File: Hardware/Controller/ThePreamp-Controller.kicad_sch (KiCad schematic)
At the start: 17 parts, among them J1 8V, J2 Digital Out, J3 SPI DISPLAY 1, J4 SPI DISPLAY 2, J5 Power relay trigger, SW1 RotaryEncoder_Switch, SW2 RotaryEncoder_Switch, U1 CAT24C64WI-GT3, U2 ESP32-DEVKIT-V1, U3 TSOP34838, U4 APC-817B1-SL

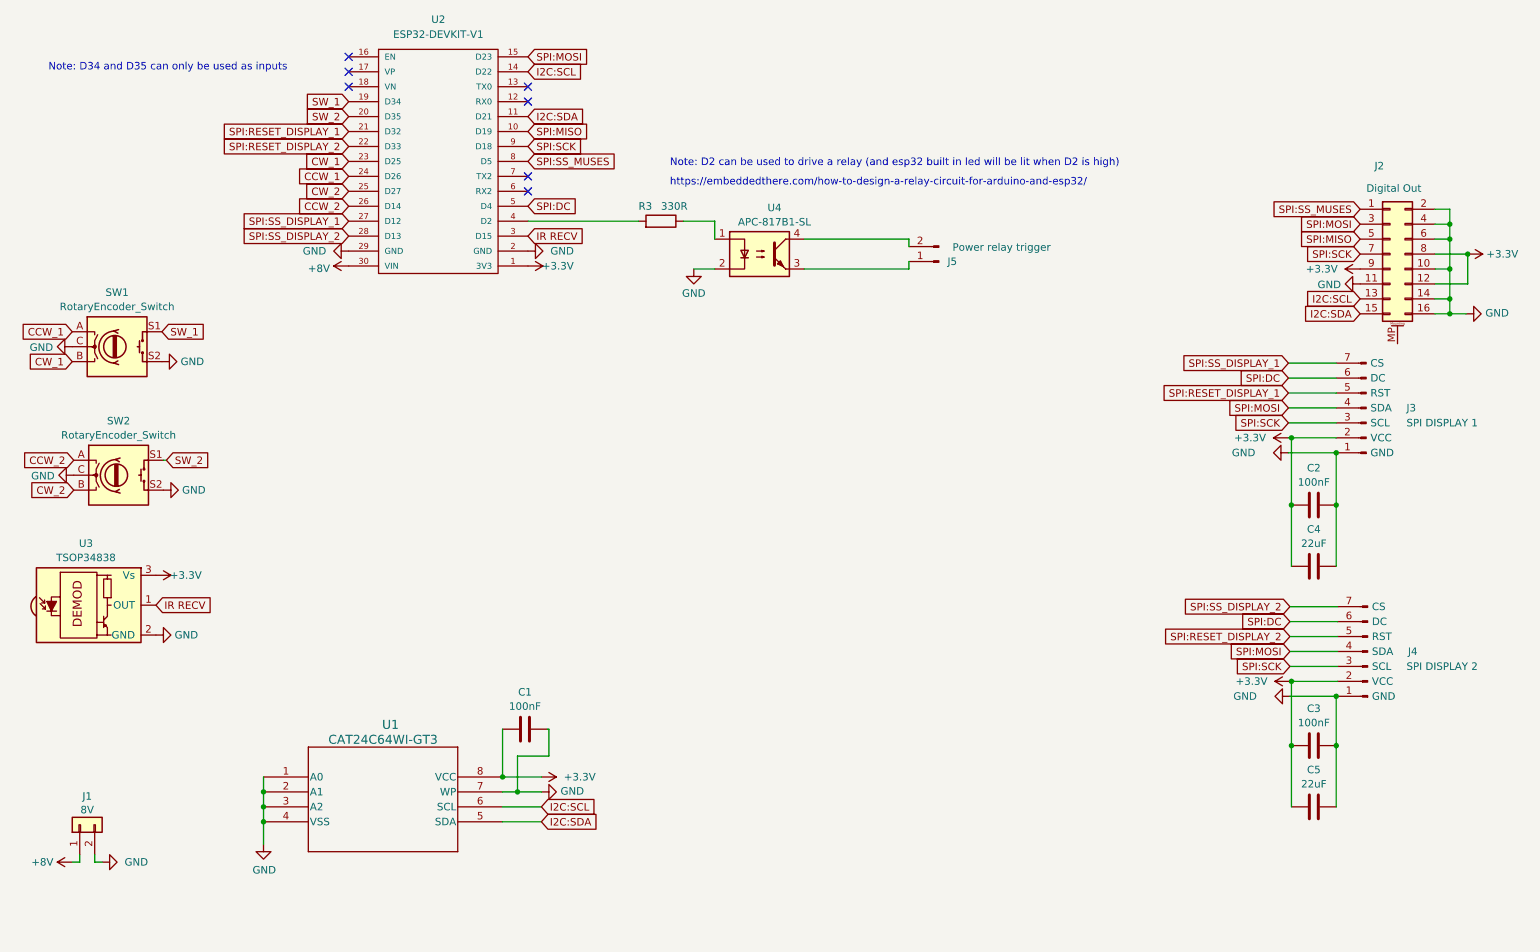
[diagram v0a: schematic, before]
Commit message: Changed power connectors
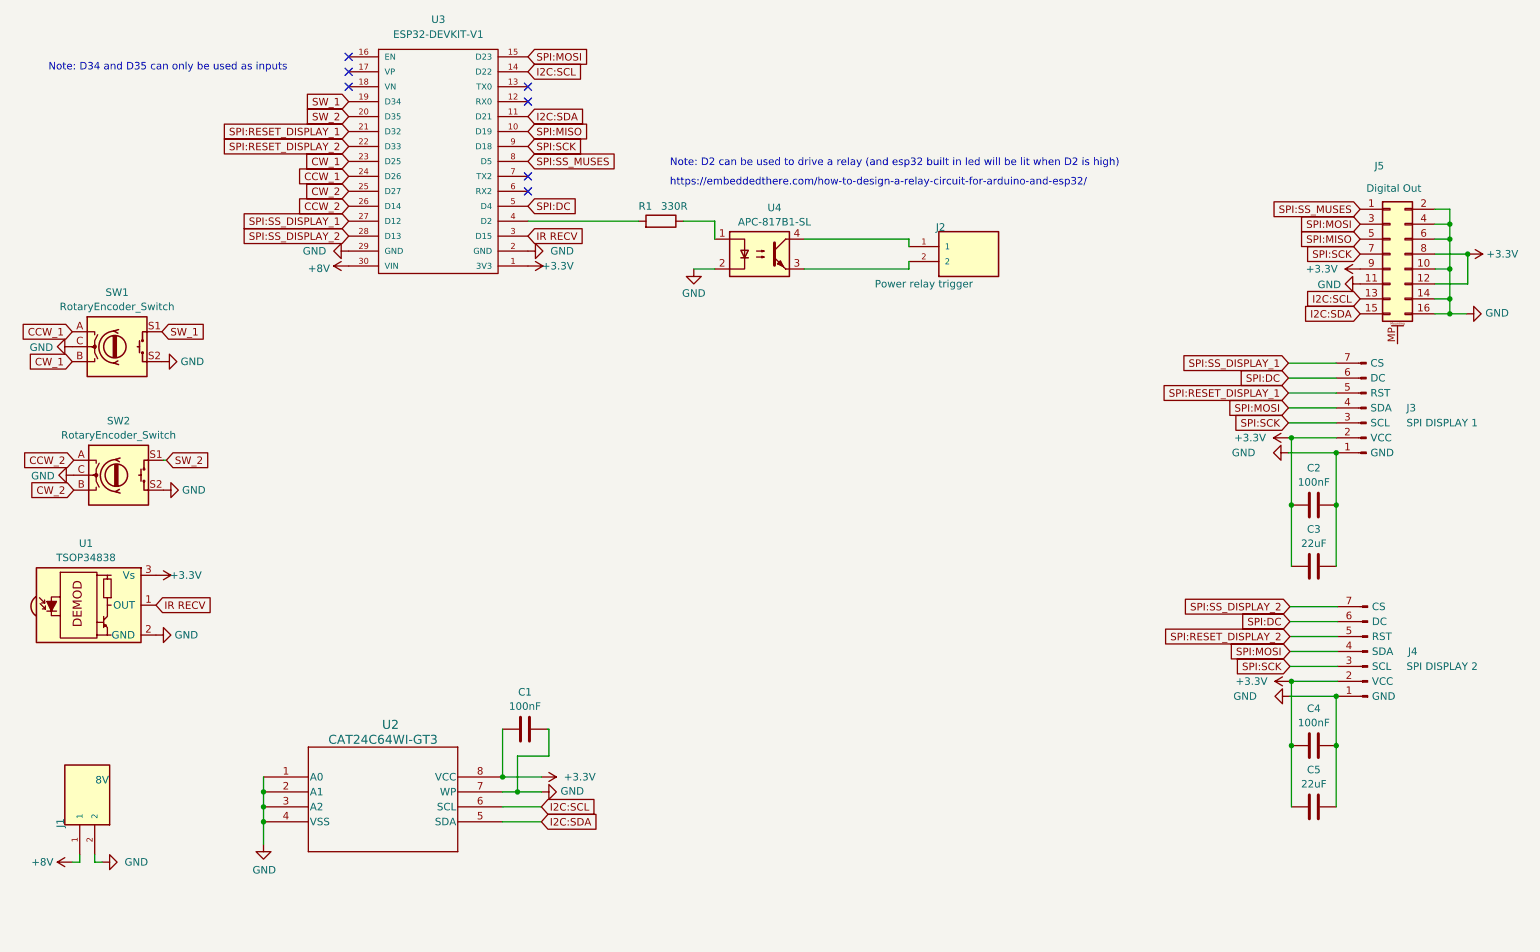
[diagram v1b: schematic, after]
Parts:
- J1: footprint TerminalBlock:TerminalBlock_bornier-2_P5.08mm -> THE_PREAMP_CONN_POWER_5_08:TBP01R2-508-02BK (VERT); symbol Connector_Generic:Conn_01x02 -> POWER_2P_VERT:TBP01R1-508-02BK; MANUFACTURER (none) -> CUI; STANDARD (none) -> Manufacturer Recommendations
- J2: renamed from J5; footprint Connector_JST:JST_XH_B2B-XH-A_1x02_P2.50mm_Vertical -> THE_PREAMP_CONN_POWER_5_08:TBP01R2-508-02BK (VERT); symbol Connector:Conn_01x02_Pin -> POWER_2P_VERT:TBP01R1-508-02BK; MANUFACTURER (none) -> CUI; STANDARD (none) -> Manufacturer Recommendations
- renumbered C4 to C3, C3 to C4, J2 to J5, R3 to R1, U3 to U1, U1 to U2, U2 to U3
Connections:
- net at U4.3: now also J2.2; no longer J2.1 (Pin_1)
- net at U4.4: now also J2.1; no longer J2.2 (Pin_2)
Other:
- moved on the sheet: J1

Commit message: Ready for production
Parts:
- added C6: 100uF, Capacitor_THT:CP_Radial_D8.0mm_P3.50mm, symbol Device:C_Polarized
- added J6: 3.3V (Opt), THE_PREAMP_CONN_POWER_5_08:TBP01R2-508-02BK (VERT), symbol POWER_2P_VERT:TBP01R1-508-02BK
- added J7: Conn_01x03_Pin, Connector_PinHeader_2.54mm:PinHeader_1x03_P2.54mm_Vertical, symbol Connector:Conn_01x03_Pin
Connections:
- net +3V3: now also J7.2 (Pin_2); no longer C1.1, U2.8 (VCC), U3.1 (3V3)
- net +8V: now also C6.1
- net GND: now also C6.2, J6.2
- net at U4.3: now also J2.1; no longer J2.2
- net at U4.4: now also J2.2; no longer J2.1
- new net: J6.1, J7.3 (Pin_3)
- new net +3V3 ESP32: C1.1, J7.1 (Pin_1), U2.8 (VCC), U3.1 (3V3)
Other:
- moved on the sheet: C1, J1, J2, U2, U4

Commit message: Updated Template-Daughter-board to reflect changes
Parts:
- added R2, R3: 2K2, Resistor_SMD:R_0805_2012Metric_Pad1.20x1.40mm_HandSolder, symbol Device:R
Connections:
- net +3V3 ESP32: now also R2.2, R3.2
- net I2C:SCL: now also R2.1
- net I2C:SDA: now also R3.1

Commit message: Pcb dimensions
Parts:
- added J8: 12V, THE_PREAMP_CONN_POWER_5_08:TBP01R2-508-02BK (VERT), symbol POWER_2P_VERT:TBP01R1-508-02BK
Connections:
- net GND: now also J8.2; no longer J5.14 (Pin_14), J5.16 (Pin_16)
- new net +12V: J5.14 (Pin_14), J5.16 (Pin_16), J8.1

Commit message: Chassis placement new draft
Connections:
- net +12V: now also J5.2 (Pin_2), J5.4 (Pin_4), J5.6 (Pin_6); no longer J5.14 (Pin_14), J5.16 (Pin_16)
- net +3V3: now also J5.10 (Pin_10)
- net GND: now also J5.14 (Pin_14), J5.16 (Pin_16); no longer J5.10 (Pin_10), J5.2 (Pin_2), J5.4 (Pin_4), J5.6 (Pin_6)
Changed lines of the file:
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@@
 	)
 	(junction
-		(at 263.906 62.484)
+		(at 263.906 73.914)
+		(diameter 0)
+		(color 0 0 0 0)
+	)
+	(junction
+		(at 263.906 59.944)
 		(diameter 0)
 		(color 0 0 0 0)
@@
 	)
 	(junction
-		(at 266.954 65.024)
+		(at 263.906 67.564)
 		(diameter 0)
 		(color 0 0 0 0)
@@
 	)
 	(junction
-		(at 264.16 72.644)
-		(diameter 0)
-		(color 0 0 0 0)
-	)
-	(junction
 		(at 117.856 153.67)
 		(diameter 0)
@@
 	)
 	(junction
-		(at 263.906 59.944)
-		(diameter 0)
-		(color 0 0 0 0)
-	)
-	(junction
 		(at 120.396 156.21)
 		(diameter 0)
@@
 	(wire
 		(pts
+			(xy 263.906 65.024) (xy 263.906 67.564)
+		)
+		(stroke
+			(width 0)
+			(type default)
+		)
+	)
+	(wire
+		(pts
+			(xy 263.906 62.484) (xy 263.906 59.944)
+		)
+		(stroke
+			(width 0)
+			(type default)
+		)
+	)
+	(wire
+		(pts
 			(xy 69.596 67.056) (xy 71.882 67.056)
 		)
@@
 	(wire
 		(pts
-			(xy 154.94 66.04) (xy 167.64 66.04)
+			(xy 263.906 57.404) (xy 263.906 59.944)
 		)
 		(stroke
@@
 	(wire
 		(pts
-			(xy 165.1 63.5) (xy 167.64 63.5)
+			(xy 154.94 66.04) (xy 167.64 66.04)
 		)
 		(stroke
@@
 	(wire
 		(pts
-			(xy 124.46 158.75) (xy 117.856 158.75)
+			(xy 165.1 63.5) (xy 167.64 63.5)
 		)
 		(stroke
@@
 	(wire
 		(pts
-			(xy 261.366 72.644) (xy 264.16 72.644)
+			(xy 124.46 158.75) (xy 117.856 158.75)
 		)
 		(stroke
@@
 	(wire
 		(pts
-			(xy 263.906 57.404) (xy 263.906 59.944)
+			(xy 261.366 75.184) (xy 263.906 75.184)
 		)
 		(stroke
@@
 	(wire
 		(pts
-			(xy 263.906 62.484) (xy 263.906 67.564)
+			(xy 263.906 67.564) (xy 263.906 70.104)
 		)
 		(stroke
@@
 	(wire
 		(pts
-			(xy 264.16 75.184) (xy 264.16 72.644)
-		)
-		(stroke
-			(width 0)
-			(type default)
-		)
-	)
-	(wire
-		(pts
 			(xy 236.474 93.726) (xy 244.602 93.726)
 		)
@@
 	(wire
 		(pts
-			(xy 261.366 75.184) (xy 264.16 75.184)
+			(xy 155.702 32.766) (xy 159.766 32.766)
 		)
 		(stroke
@@
 	(wire
 		(pts
-			(xy 155.702 32.766) (xy 159.766 32.766)
+			(xy 236.474 96.266) (xy 236.982 96.266)
 		)
 		(stroke
@@
 	(wire
 		(pts
-			(xy 236.474 96.266) (xy 236.982 96.266)
+			(xy 263.906 72.644) (xy 263.906 73.914)
 		)
 		(stroke
@@
 	(wire
 		(pts
-			(xy 261.366 70.104) (xy 266.954 70.104)
+			(xy 261.366 70.104) (xy 263.906 70.104)
 		)
 		(stroke
@@
 	(wire
 		(pts
-			(xy 263.906 59.944) (xy 263.906 62.484)
+			(xy 125.73 145.542) (xy 125.73 150.114)
 		)
 		(stroke
@@
 	(wire
 		(pts
-			(xy 125.73 145.542) (xy 125.73 150.114)
+			(xy 45.212 100.076) (xy 45.72 100.076)
 		)
 		(stroke
@@
 	(wire
 		(pts
-			(xy 45.212 100.076) (xy 45.72 100.076)
+			(xy 236.728 127.508) (xy 244.856 127.508)
 		)
 		(stroke
@@
 	(wire
 		(pts
-			(xy 236.728 127.508) (xy 244.856 127.508)
+			(xy 261.366 62.484) (xy 263.906 62.484)
 		)
 		(stroke
@@
 	(wire
 		(pts
-			(xy 261.366 62.484) (xy 263.906 62.484)
+			(xy 236.982 107.696) (xy 236.982 118.11)
 		)
 		(stroke
@@
 	(wire
 		(pts
-			(xy 236.982 107.696) (xy 236.982 118.11)
+			(xy 88.9 125.222) (xy 90.17 125.222)
 		)
 		(stroke
@@
 	(wire
 		(pts
-			(xy 88.9 125.222) (xy 90.17 125.222)
+			(xy 77.216 153.67) (xy 77.216 156.21)
 		)
 		(stroke
@@
 	(wire
 		(pts
-			(xy 77.216 153.67) (xy 77.216 156.21)
+			(xy 263.906 73.914) (xy 263.906 75.184)
 		)
 		(stroke
@@
 	(wire
 		(pts
-			(xy 266.954 65.024) (xy 266.954 70.104)
-		)
-		(stroke
-			(width 0)
-			(type default)
-		)
-	)
-	(wire
-		(pts
 			(xy 124.46 156.21) (xy 120.396 156.21)
 		)
@@
 	(wire
 		(pts
-			(xy 261.366 65.024) (xy 266.954 65.024)
+			(xy 261.366 65.024) (xy 263.906 65.024)
 		)
 		(stroke
@@
 	(wire
 		(pts
+			(xy 261.366 72.644) (xy 263.906 72.644)
+		)
+		(stroke
+			(width 0)
+			(type default)
+		)
+	)
+	(wire
+		(pts
 			(xy 86.36 125.222) (xy 86.36 123.952)
 		)
@@
 	(symbol
 		(lib_id "power:+12V")
-		(at 264.16 72.644 270)
+		(at 263.906 59.944 270)
 		(unit 1)
 		(exclude_from_sim no)
@@
 		(fields_autoplaced yes)
 		(property "Reference" "#PWR031"
-			(at 260.35 72.644 0)
+			(at 260.096 59.944 0)
 			(effects
 				(font
@@
 		)
 		(property "Value" "+12V"
-			(at 267.335 72.644 90)
+			(at 267.081 59.944 90)
 			(effects
 				(font
@@
 		)
 		(property "Footprint" ""
-			(at 264.16 72.644 0)
+			(at 263.906 59.944 0)
 			(effects
 				(font
@@
 		)
 		(property "Datasheet" ""
-			(at 264.16 72.644 0)
+			(at 263.906 59.944 0)
 			(effects
 				(font
@@
 		)
 		(property "Description" "Power symbol creates a global label with name \"+12V\""
-			(at 264.16 72.644 0)
+			(at 263.906 59.944 0)
 			(effects
 				(font
@@
 	(symbol
 		(lib_id "power:GND")
-		(at 263.906 59.944 90)
+		(at 263.906 73.914 90)
 		(unit 1)
 		(exclude_from_sim no)
@@
 		(dnp no)
 		(property "Reference" "#PWR023"
-			(at 270.256 59.944 0)
+			(at 270.256 73.914 0)
 			(effects
 				(font
@@
 		)
 		(property "Value" "GND"
-			(at 267.1572 59.817 90)
+			(at 267.1572 73.787 90)
 			(effects
 				(font
@@
 		)
 		(property "Footprint" ""
-			(at 263.906 59.944 0)
+			(at 263.906 73.914 0)
 			(effects
 				(font
@@
 		)
 		(property "Datasheet" ""
-			(at 263.906 59.944 0)
+			(at 263.906 73.914 0)
 			(effects
 				(font
@@
 		)
 		(property "Description" ""
-			(at 263.906 59.944 0)
+			(at 263.906 73.914 0)
 			(effects
 				(font
@@
 	(symbol
 		(lib_id "power:+3.3V")
-		(at 266.954 65.024 270)
+		(at 263.906 67.564 270)
 		(unit 1)
 		(exclude_from_sim no)
@@
 		(fields_autoplaced yes)
 		(property "Reference" "#PWR024"
-			(at 263.144 65.024 0)
+			(at 260.096 67.564 0)
 			(effects
 				(font
@@
 		)
 		(property "Value" "+3V3"
-			(at 270.129 65.024 90)
+			(at 267.081 67.564 90)
 			(effects
 				(font
@@
 		)
 		(property "Footprint" ""
-			(at 266.954 65.024 0)
+			(at 263.906 67.564 0)
 			(effects
 				(font
@@
 		)
 		(property "Datasheet" ""
-			(at 266.954 65.024 0)
+			(at 263.906 67.564 0)
 			(effects
 				(font
@@
 		)
 		(property "Description" ""
-			(at 266.954 65.024 0)
+			(at 263.906 67.564 0)
 			(effects
 				(font

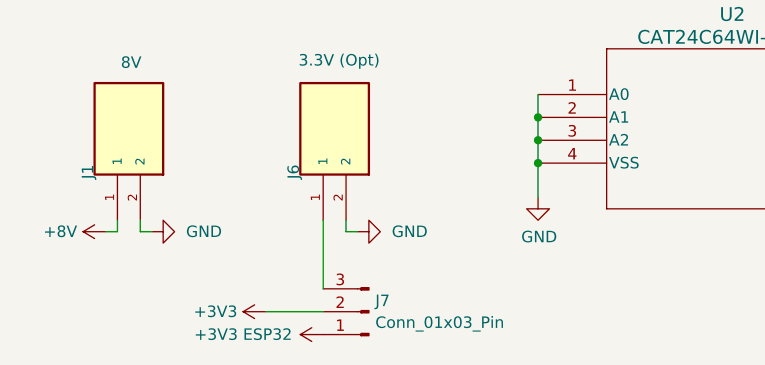
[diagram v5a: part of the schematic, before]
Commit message: Updated pcb 3.3V + adjust of connectors on controller pcb
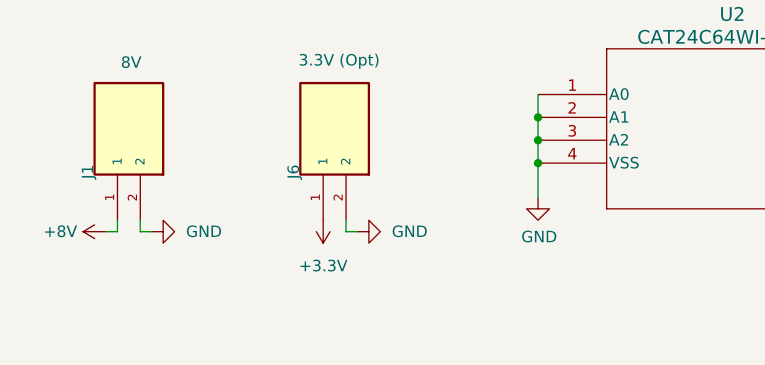
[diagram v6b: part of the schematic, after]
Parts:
- removed J7: Conn_01x03_Pin, Connector_PinHeader_2.54mm:PinHeader_1x03_P2.54mm_Vertical, symbol Connector:Conn_01x03_Pin
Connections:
- net +3.3V: now reaches J6.1
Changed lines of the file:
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@@
 	(wire
 		(pts
-			(xy 46.99 177.8) (xy 53.34 177.8)
-		)
-		(stroke
-			(width 0)
-			(type default)
-		)
-	)
-	(wire
-		(pts
 			(xy 236.982 148.59) (xy 236.982 159.004)
 		)
@@
 	(wire
 		(pts
-			(xy 53.34 167.64) (xy 53.34 175.26)
-		)
-		(stroke
-			(width 0)
-			(type default)
-		)
-	)
-	(wire
-		(pts
 			(xy 236.474 83.566) (xy 244.602 83.566)
 		)
@@
 	)
 	(symbol
+		(lib_name "+3.3V_1")
+		(lib_id "power:+3.3V")
+		(at 53.34 167.64 180)
+		(unit 1)
+		(exclude_from_sim no)
+		(in_bom yes)
+		(on_board yes)
+		(dnp no)
+		(fields_autoplaced yes)
+		(property "Reference" "#PWR025"
+			(at 53.34 163.83 0)
+			(effects
+				(font
+					(size 1.27 1.27)
+				)
+				(hide yes)
+			)
+		)
+		(property "Value" "+3.3V"
+			(at 53.34 172.72 0)
+			(effects
+				(font
+					(size 1.27 1.27)
+				)
+			)
+		)
+		(property "Footprint" ""
+			(at 53.34 167.64 0)
+			(effects
+				(font
+					(size 1.27 1.27)
+				)
+				(hide yes)
+			)
+		)
+		(property "Datasheet" ""
+			(at 53.34 167.64 0)
+			(effects
+				(font
+					(size 1.27 1.27)
+				)
+				(hide yes)
+			)
+		)
+		(property "Description" "Power symbol creates a global label with name \"+3.3V\""
+			(at 53.34 167.64 0)
+			(effects
+				(font
+					(size 1.27 1.27)
+				)
+				(hide yes)
+			)
+		)
+		(pin "1"
+		)
+		(instances
+			(project "ThePreamp-Controller"
+				(path "/f6c644f4-3036-41a6-9e14-2c08c079c6cd"
+					(reference "#PWR025")
+					(unit 1)
+				)
+			)
+		)
+	)
+	(symbol
 		(lib_id "power:GND")
 		(at 43.942 129.794 90)
@@
 	)
 	(symbol
-		(lib_id "Connector:Conn_01x03_Pin")
-		(at 58.42 177.8 180)
-		(unit 1)
-		(exclude_from_sim no)
-		(in_bom yes)
-		(on_board yes)
-		(dnp no)
-		(fields_autoplaced yes)
-		(property "Reference" "J7"
-			(at 59.1312 176.5878 0)
-			(effects
-				(font
-					(size 1.27 1.27)
-				)
-				(justify right)
-			)
-		)
-		(property "Value" "Conn_01x03_Pin"
-			(at 59.1312 179.0121 0)
-			(effects
-				(font
-					(size 1.27 1.27)
-				)
-				(justify right)
-			)
-		)
-		(property "Footprint" "Connector_PinHeader_2.54mm:PinHeader_1x03_P2.54mm_Vertical"
-			(at 58.42 177.8 0)
-			(effects
-				(font
-					(size 1.27 1.27)
-				)
-				(hide yes)
-			)
-		)
-		(property "Datasheet" "~"
-			(at 58.42 177.8 0)
-			(effects
-				(font
-					(size 1.27 1.27)
-				)
-				(hide yes)
-			)
-		)
-		(property "Description" "Generic connector, single row, 01x03, script generated"
-			(at 58.42 177.8 0)
-			(effects
-				(font
-					(size 1.27 1.27)
-				)
-				(hide yes)
-			)
-		)
-		(pin "2"
-		)
-		(pin "3"
-		)
-		(pin "1"
-		)
-		(instances
-			(project "ThePreamp-Controller"
-				(path "/f6c644f4-3036-41a6-9e14-2c08c079c6cd"
-					(reference "J7")
-					(unit 1)
-				)
-			)
-		)
-	)
-	(symbol
 		(lib_id "power:GND")
 		(at 263.906 73.914 90)
@@
 	)
 	(symbol
-		(lib_id "power:+3.3V")
-		(at 53.34 180.34 90)
-		(unit 1)
-		(exclude_from_sim no)
-		(in_bom yes)
-		(on_board yes)
-		(dnp no)
-		(property "Reference" "#PWR027"
-			(at 57.15 180.34 0)
-			(effects
-				(font
-					(size 1.27 1.27)
-				)
-				(hide yes)
-			)
-		)
-		(property "Value" "+3V3 ESP32"
-			(at 44.45 180.34 90)
-			(effects
-				(font
-					(size 1.27 1.27)
-				)
-			)
-		)
-		(property "Footprint" ""
-			(at 53.34 180.34 0)
-			(effects
-				(font
-					(size 1.27 1.27)
-				)
-				(hide yes)
-			)
-		)
-		(property "Datasheet" ""
-			(at 53.34 180.34 0)
-			(effects
-				(font
-					(size 1.27 1.27)
-				)
-				(hide yes)
-			)
-		)
-		(property "Description" ""
-			(at 53.34 180.34 0)
-			(effects
-				(font
-					(size 1.27 1.27)
-				)
-				(hide yes)
-			)
-		)
-		(pin "1"
-		)
-		(instances
-			(project "ThePreamp-Controller"
-				(path "/f6c644f4-3036-41a6-9e14-2c08c079c6cd"
-					(reference "#PWR027")
-					(unit 1)
-				)
-			)
-		)
-	)
-	(symbol
 		(lib_id "POWER_2P_VERT:TBP01R1-508-02BK")
 		(at 33.02 157.48 90)
@@
 					(unit 1)
 				)
-			)
-		)
-	)
-	(symbol
-		(lib_name "+3.3V_1")
-		(lib_id "power:+3.3V")
-		(at 46.99 177.8 90)
-		(unit 1)
-		(exclude_from_sim no)
-		(in_bom yes)
-		(on_board yes)
-		(dnp no)
-		(fields_autoplaced yes)
-		(property "Reference" "#PWR025"
-			(at 50.8 177.8 0)
-			(effects
-				(font
-					(size 1.27 1.27)
-				)
-				(hide yes)
-			)
-		)
-		(property "Value" "+3V3"
-			(at 43.815 177.8 90)
-			(effects
-				(font
-					(size 1.27 1.27)
-				)
-				(justify left)
-			)
-		)
-		(property "Footprint" ""
-			(at 46.99 177.8 0)
-			(effects
-				(font
-					(size 1.27 1.27)
-				)
-				(hide yes)
-			)
-		)
-		(property "Datasheet" ""
-			(at 46.99 177.8 0)
-			(effects
-				(font
-					(size 1.27 1.27)
-				)
-				(hide yes)
-			)
-		)
-		(property "Description" "Power symbol creates a global label with name \"+3.3V\""
-			(at 46.99 177.8 0)
-			(effects
-				(font
-					(size 1.27 1.27)
-				)
-				(hide yes)
-			)
-		)
-		(pin "1"
-		)
-		(instances
-			(project "ThePreamp-Controller"
-				(path "/f6c644f4-3036-41a6-9e14-2c08c079c6cd"
-					(reference "#PWR025")
-					(unit 1)
-				)

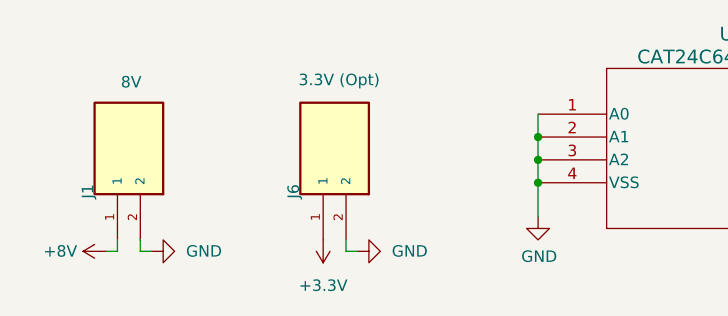
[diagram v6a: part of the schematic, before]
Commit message: Ready for review (updated Digital PSU - Transformer and Controller)
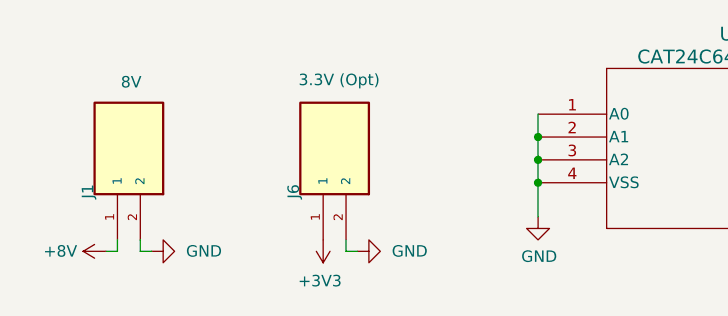
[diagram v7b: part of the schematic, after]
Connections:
- net +3.3V is gone; now on net +3V3: J6.1
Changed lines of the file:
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@@
 		(on_board yes)
 		(dnp no)
-		(fields_autoplaced yes)
 		(property "Reference" "#PWR025"
 			(at 53.34 163.83 0)
@@
 			)
 		)
-		(property "Value" "+3.3V"
-			(at 53.34 172.72 0)
+		(property "Value" "+3V3"
+			(at 50.546 172.212 0)
 			(effects
 				(font
 					(size 1.27 1.27)
 				)
+				(justify right)
 			)
 		)
